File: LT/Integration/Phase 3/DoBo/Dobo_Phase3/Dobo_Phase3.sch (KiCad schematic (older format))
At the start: 3 parts, among them J2 Conn_01x02_Female, J4 Conn_01x02_Female, J46 Bus

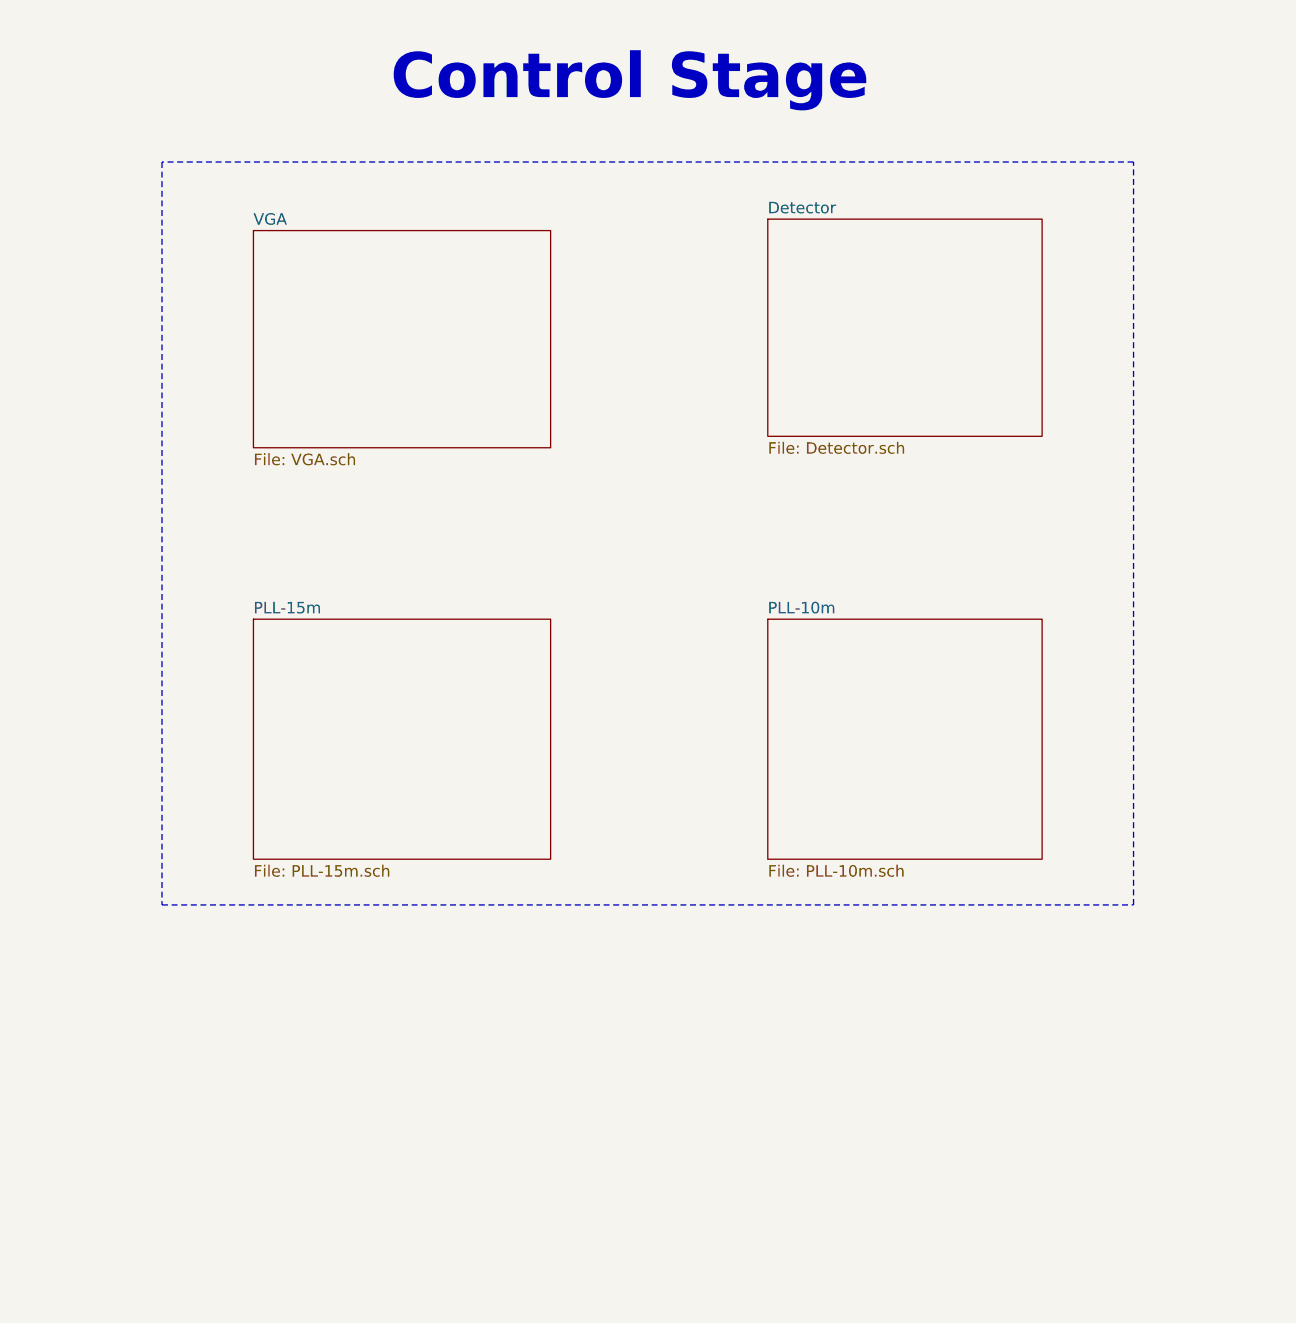
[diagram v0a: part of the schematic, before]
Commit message: Added the MotherBoard File for Phase 3 and renamed the Presentation Folder
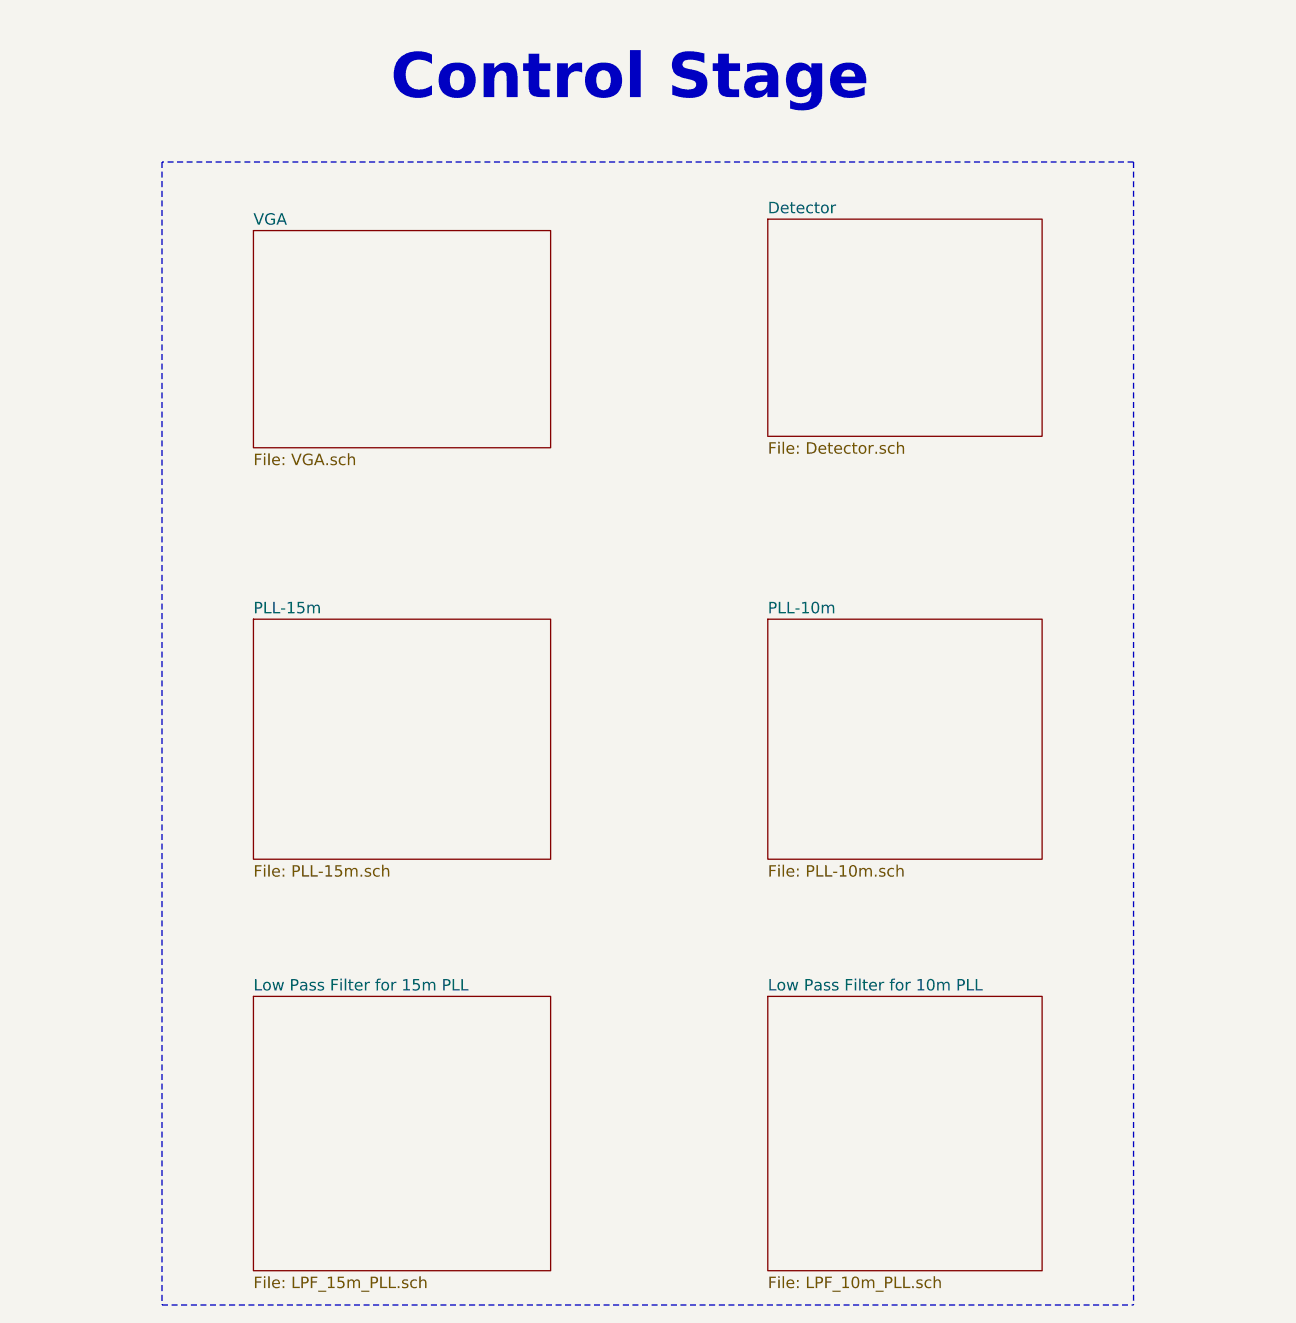
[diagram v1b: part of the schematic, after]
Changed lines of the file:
@@
 $Descr A3 16535 11693
 encoding utf-8
-Sheet 1 8
+Sheet 1 10
 Title ""
 Date ""
@@
 $EndSheet
 Wire Notes Line width 39 style solid
-	6400 6000 6400 9250
-Wire Notes Line width 39 style solid
-	6400 9250 10650 9250
-Wire Notes Line width 39 style solid
-	10650 9250 10650 6000
+	6400 11000 10650 11000
 Wire Notes Line width 39 style solid
 	10650 6000 6400 6000
@@
 Wire Wire Line
 	4100 7400 4050 7400
+$Sheet
+S 6800 9650 1300 1200
+U 5EB6970C
+F0 "Low Pass Filter for 15m PLL" 50
+F1 "LPF_15m_PLL.sch" 50
+$EndSheet
+$Sheet
+S 9050 9650 1200 1200
+U 5EB6A002
+F0 "Low Pass Filter for 10m PLL" 50
+F1 "LPF_10m_PLL.sch" 50
+$EndSheet
+Wire Notes Line width 39 style solid
+	6400 6000 6400 11000
+Wire Notes Line width 39 style solid
+	10650 6000 10650 11000
 $EndSCHEMATC

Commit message: Added the completed layout for the DoBo Phase 3
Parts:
- removed J2, J4: Conn_01x02_Female, Connector_PinSocket_2.54mm:PinSocket_1x02_P2.54mm_Vertical, symbol Connector:Conn_01x02_Female
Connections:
- net labels added: 10m_PLL_Output, 15m_PLL_Output, Detector_input, Down_Mixer-IF_Filter, Down_Mixer_Input, IF_Filter-VGA, IF_Filter_Input, IF_Filter_Output, LPF-Down_Mixer, LPF-Up_Mixer, Local_Oscillator_Output, PLL_10m_LPF, PLL_15m-LPF, Up_Mixer_Output, Up_Mixer_input, VGA-Detector, VGA-Up_Mixer, VGA_Output, VGA_input
- net labels removed: GND, IF_Output
- wire segments 6 -> 20
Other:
- note added: "10m_PLL"
- note added: "15m_PLL"
- note added: "Detector"
- note added: "Down-Mixer"
- note added: "IF Filter\n"
- note added: "LPF_10m_PLL"
- note added: "LPF_15m_PLL"
- note added: "PCB 10"
- note added: "PCB 11"
- note added: "PCB 12"
- note added: "PCB 4"
- note added: "PCB 5"
- note added: "PCB 6"
- note added: "PCB 7"
- note added: "PCB 8"
- note added: "PCB 9"
- note added: "Up-Mixer"
- note added: "VGA"

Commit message: Adding the DoBo Phase 3 integration with all traces routed
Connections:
- net labels added: +5V, +8V, -5V, Bus_100, Bus_104, Bus_114, Bus_85, Bus_87, Bus_89, Bus_94, Bus_96, Bus_99, GND, LNA_Output, LPF_Input
- net labels removed: 10m_PLL_Output, 15m_PLL_Output, Detector_input, Down_Mixer_Input, Down_Mixer_Output, IF_Filter_Input, IF_Filter_Output, Local_Oscillator_Output, Up_Mixer_Output, Up_Mixer_input, VGA_Output, VGA_input
- wire segments 20 -> 40
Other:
- note added: "Daughter Board"
- note added: "Microwire\nInterface"
- note removed: "Control Stage"
- note removed: "Intermediate Stage"
- note removed: "Step-Daughter Board"

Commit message: Fixed the hierarchy for the MoBo Phase 3
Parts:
- J46: symbol SS:Bus -> Dobo_Phase3-rescue:Bus-SS
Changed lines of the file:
@@
 $EndDescr
 $Comp
-L SS:Bus J46
+L Dobo_Phase3-rescue:Bus-SS J46
 U 1 1 5EAFD80A
 P 18500 8900
@@
 $EndComp
 $Comp
-L SS:Bus J46
+L Dobo_Phase3-rescue:Bus-SS J46
 U 2 1 5EB2EAA0
 P 18500 9800
@@
 $EndComp
 $Comp
-L SS:Bus J46
+L Dobo_Phase3-rescue:Bus-SS J46
 U 3 1 5EB3328A
 P 18500 10750
@@
 Bus_89
 $Comp
-L SS:Bus J46
+L Dobo_Phase3-rescue:Bus-SS J46
 U 4 1 5EB34CE3
 P 18500 12000

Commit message: Added the finalized layouts for the Mobo and Dobo Phase 3, as well as the preliminary layout for Phase 4 of both boards
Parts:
- added J12: Conn_01x03_Male, Connector_PinHeader_2.54mm:PinHeader_1x03_P2.54mm_Vertical, symbol Connector:Conn_01x03_Male
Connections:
- net +5V: now also J12.3 (Pin_3)
- net +8V: now also J12.1 (Pin_1)
- net -5V: now also J12.2 (Pin_2)
- net Bus_64: now reaches J46.64
- net Bus_90: now reaches J46.90 (GND)
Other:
- note added: "5/12/20"
- note added: "DoBo_Phase3"
- note added: "Rev0"
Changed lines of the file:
@@
 Text Notes 12000 9650 0    118  ~ 24
 PCB 10
-Text Notes 18950 6600 0    118  ~ 24
-PCB 12
 Text Notes 17750 3800 0    118  ~ 24
 PCB 9
@@
 Text Label 15600 3600 2    50   ~ 0
 VGA-Detector
-Text Label 16300 6400 2    50   ~ 0
-LPF-Up_Mixer
 $Sheet
 S 6950 8200 2200 1500
@@
 F6 "LE" I L 3800 9350 50
 $EndSheet
-$Sheet
-S 16400 5050 3250 1600
-U 5EAF3CBD
-F0 "Up-Mixer" 20
-F1 "Up-Mixer.sch" 20
-F2 "Local_Oscillator_Input" I L 16400 6400 79
-F3 "Up_Mixer_Output" O R 19650 5500 79
-F4 "Up_Mixer_Input" I L 16400 5500 79
-$EndSheet
-Text Notes 17400 5000 0    197  ~ 39
-Up-Mixer
 Wire Wire Line
 	9150 8600 9350 8600
@@
 	15400 8500 15750 8500
 Wire Wire Line
-	15750 6400 16400 6400
-Wire Wire Line
 	15750 6400 15750 8500
 Wire Wire Line
@@
 Wire Wire Line
 	14700 3600 16450 3600
-Connection ~ 14700 5500
-Wire Wire Line
-	14700 5500 16400 5500
 $Sheet
 S 4000 5050 3250 1600
@@
 Wire Wire Line
 	11350 6900 11500 6900
-Text HLabel 20650 5500 2    79   Output ~ 0
-LPF_Input
-Wire Wire Line
-	19650 5500 20650 5500
 Text HLabel 3150 5500 0    79   Input ~ 0
 LNA_Output
 Wire Wire Line
-	3150 5500 4000 5500
+	3150 5500 3350 5500
 Wire Wire Line
 	6250 9000 6950 9000
@@
 $EndComp
 Wire Wire Line
-	19850 10750 19850 10800
-Wire Wire Line
 	19650 10750 19650 10800
 Wire Wire Line
@@
 Wire Wire Line
 	19350 12000 19350 12050
+$Comp
+L Connector:Conn_01x03_Male J12
+U 1 1 5ECA6C19
+P 18000 13350
+F 0 "J12" H 18108 13631 50  0000 C CNN
+F 1 "Conn_01x03_Male" H 17650 13350 50  0000 C CNN
+F 2 "Connector_PinHeader_2.54mm:PinHeader_1x03_P2.54mm_Vertical" H 18000 13350 50  0001 C CNN
+F 3 "~" H 18000 13350 50  0001 C CNN
+	1    18000 13350
+	1    0    0    -1
+$EndComp
+$Comp
+L power:+8V #PWR0180
+U 1 1 5EC95943
+P 18250 13250
+F 0 "#PWR0180" H 18250 13100 50  0001 C CNN
+F 1 "+8V" H 18265 13423 50  0000 C CNN
+F 2 "" H 18250 13250 50  0001 C CNN
+F 3 "" H 18250 13250 50  0001 C CNN
+	1    18250 13250
+	1    0    0    -1
+$EndComp
+Wire Wire Line
+	18200 13250 18250 13250
+Wire Wire Line
+	18200 13350 18350 13350
+$Comp
+L power:+5V #PWR0178
+U 1 1 5EC946AC
+P 18200 13450
+F 0 "#PWR0178" H 18200 13300 50  0001 C CNN
+F 1 "+5V" H 18215 13623 50  0000 C CNN
+F 2 "" H 18200 13450 50  0001 C CNN
+F 3 "" H 18200 13450 50  0001 C CNN
+	1    18200 13450
+	-1   0    0    1
+$EndComp
+$Comp
+L power:-5V #PWR0179
+U 1 1 5EC95083
+P 18350 13350
+F 0 "#PWR0179" H 18350 13450 50  0001 C CNN
+F 1 "-5V" H 18365 13523 50  0000 C CNN
+F 2 "" H 18350 13350 50  0001 C CNN
+F 3 "" H 18350 13350 50  0001 C CNN
+	1    18350 13350
+	-1   0    0    1
+$EndComp
+Connection ~ 14700 5500
+Wire Wire Line
+	19650 5500 20550 5500
+Text HLabel 20650 5500 2    79   Output ~ 0
+LPF_Input
+Wire Wire Line
+	14700 5500 16400 5500
+Wire Wire Line
+	15750 6400 16400 6400
+Text Notes 17400 5000 0    197  ~ 39
+Up-Mixer
+$Sheet
+S 16400 5050 3250 1600
+U 5EAF3CBD
+F0 "Up-Mixer" 20
+F1 "Up-Mixer.sch" 20
+F2 "Local_Oscillator_Input" I L 16400 6400 79
+F3 "Up_Mixer_Output" O R 19650 5500 79
+F4 "Up_Mixer_Input" I L 16400 5500 79
+$EndSheet
+Text Label 16300 6400 2    50   ~ 0
+LPF-Up_Mixer
+Text Notes 18950 6600 0    118  ~ 24
+PCB 12
+Text Notes 22350 15900 0    50   ~ 0
+Rev0
+Text Notes 19850 15900 0    50   ~ 0
+5/12/20
+Text Notes 19150 15750 0    50   ~ 0
+DoBo_Phase3
+Text GLabel 19950 10800 3    28   Input ~ 0
+Bus_90
+Wire Wire Line
+	19950 10750 19950 10800
+Wire Wire Line
+	19850 10750 19850 10800
+Text GLabel 17350 10800 3    28   Input ~ 0
+Bus_64
+Wire Wire Line
+	17350 10750 17350 10800
+Text GLabel 3250 5750 0    79   Input ~ 0
+Bus_90
+Wire Wire Line
+	3250 5750 3350 5750
+Wire Wire Line
+	3350 5750 3350 5500
+Connection ~ 3350 5500
+Wire Wire Line
+	3350 5500 4000 5500
+Text GLabel 20650 5750 2    79   Input ~ 0
+Bus_64
+Wire Wire Line
+	20550 5500 20550 5750
+Wire Wire Line
+	20550 5750 20650 5750
+Connection ~ 20550 5500
+Wire Wire Line
+	20550 5500 20650 5500
 $EndSCHEMATC
